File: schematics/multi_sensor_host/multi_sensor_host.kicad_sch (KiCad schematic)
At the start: 82 parts, among them J1 left hand 0, J10 swd, J11 stm_boot, J13 right hand 0, J14 right hand 1, J15 right hand 2, J16 right hand 3, J17 rst_mcu, J18 left hand 3, J19 left leg 0, J2 left hand 1, J20 left leg 1, J21 right lef 0, J22 right leg 1, J3 bm_cfg, J4 left hand 2, J5 tx, J6 MY_USB_B, J7 rst_bm71, J8 rx, J9 uart1, U11 MCP111, U12 BM71BLES1FC2-0B02AA, U4 MCP111, U7 MCP1603, U8 MCP73812, U9 MCP1603, Y1 Crystal

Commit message: Making changes...
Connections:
- net lh_int_0_0 is gone; now on net sda_1: J1.4
- net lh_int_0_1 is gone; now on net scl_1: J1.7
- net lh_int_1_0 is gone; now on net sda_3: J2.4
- net lh_int_1_1 is gone; now on net scl_3: J2.7
- net lh_int_2_0 is gone; now on net sda_5: J4.4
- net lh_int_2_1 is gone; now on net scl_5: J4.7
- net lh_int_3_0 is gone; now on net sda_7: J18.4
- net lh_int_3_1 is gone; now on net scl_7: J18.7
- net lh_scl_0 is gone; now on net scl_0: J1.3
- net lh_scl_1 is gone; now on net scl_2: J2.3
- net lh_scl_2 is gone; now on net scl_4: J4.3
- net lh_scl_3 is gone; now on net scl_6: J18.3
- net lh_sda_0 is gone; now on net sda_0: J1.1
- net lh_sda_1 is gone; now on net sda_2: J2.1
- net lh_sda_2 is gone; now on net sda_4: J4.1
- net lh_sda_3 is gone; now on net sda_6: J18.1
- net ll_int_0_0 is gone; now on net sda_17: J19.4
- net ll_int_0_1 is gone; now on net scl_17: J19.7
- net ll_int_1_0 is gone; now on net sda_19: J20.4
- net ll_int_1_1 is gone; now on net scl_19: J20.7
- net ll_scl_0 is gone; now on net scl_16: J19.3
- net ll_scl_1 is gone; now on net scl_18: J20.3
- net ll_sda_0 is gone; now on net sda_16: J19.1
- net ll_sda_1 is gone; now on net sda_18: J20.1
- net rh_int_0_0 is gone; now on net sda_9: J13.4
- net rh_int_0_1 is gone; now on net scl_9: J13.7
- net rh_int_1_0 is gone; now on net sda_11: J14.4
- net rh_int_1_1 is gone; now on net scl_11: J14.7
- net rh_int_2_0 is gone; now on net sda_13: J15.4
- net rh_int_2_1 is gone; now on net scl_13: J15.7
- net rh_int_3_0 is gone; now on net sda_15: J16.4
- net rh_int_3_1 is gone; now on net scl_15: J16.7
- net rh_scl_0 is gone; now on net scl_8: J13.3
- net rh_scl_1 is gone; now on net scl_10: J14.3
- net rh_scl_2 is gone; now on net scl_12: J15.3
- net rh_scl_3 is gone; now on net scl_14: J16.3
- net rh_sda_1 is gone; now on net sda_10: J14.1
- net rh_sda_2 is gone; now on net sda_12: J15.1
- net rh_sda_3 is gone; now on net sda_14: J16.1
- net rl_int_0_0 is gone; now on net sda_21: J21.4
- net rl_int_0_1 is gone; now on net scl_21: J21.7
- net rl_int_1_0 is gone; now on net sda_23: J22.4
- net rl_int_1_1 is gone; now on net scl_23: J22.7
- net rl_scl_0 is gone; now on net scl_20: J21.3
- net rl_scl_1 is gone; now on net scl_22: J22.3
- net rl_sda_0 is gone; now on net sda_20: J21.1
- net rl_sda_1 is gone; now on net sda_22: J22.1
- net rh_sda_0 renamed sca_8
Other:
- moved on the sheet: J1, J18, J19, J2, J20, J4, J5, J8

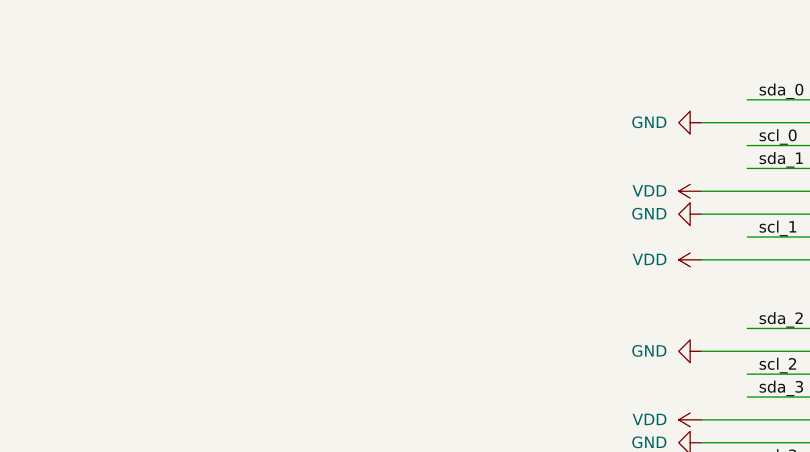
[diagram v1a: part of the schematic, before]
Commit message: 3 I2C bus, adding capacitors to sensor power lines...
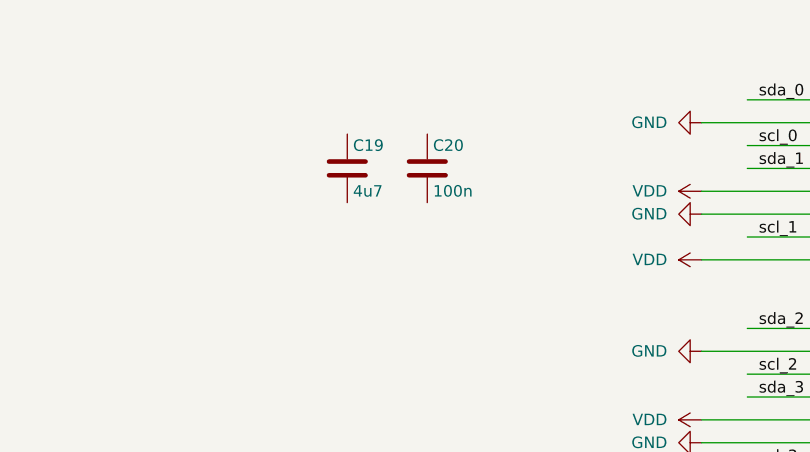
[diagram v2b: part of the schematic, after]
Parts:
- added C19: 4u7, Capacitor_SMD:C_0603_1608Metric, symbol Device:C
- added C20: 100n, Capacitor_SMD:C_0603_1608Metric, symbol Device:C
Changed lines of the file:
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@@
 	(symbol
 		(lib_id "Device:C")
+		(at 584.2 33.02 0)
+		(unit 1)
+		(exclude_from_sim no)
+		(in_bom yes)
+		(on_board yes)
+		(dnp no)
+		(property "Reference" "C19"
+			(at 584.835 30.48 0)
+			(effects
+				(font
+					(size 1.27 1.27)
+				)
+				(justify left)
+			)
+		)
+		(property "Value" "4u7"
+			(at 584.835 35.56 0)
+			(effects
+				(font
+					(size 1.27 1.27)
+				)
+				(justify left)
+			)
+		)
+		(property "Footprint" "Capacitor_SMD:C_0603_1608Metric"
+			(at 585.1652 36.83 0)
+			(effects
+				(font
+					(size 1.27 1.27)
+				)
+				(hide yes)
+			)
+		)
+		(property "Datasheet" "~"
+			(at 584.2 33.02 0)
+			(effects
+				(font
+					(size 1.27 1.27)
+				)
+				(hide yes)
+			)
+		)
+		(property "Description" "Unpolarized capacitor"
+			(at 584.2 33.02 0)
+			(effects
+				(font
+					(size 1.27 1.27)
+				)
+				(hide yes)
+			)
+		)
+		(property "URL" "https://www.digikey.com/product-detail/en/samsung-electro-mechanics-america-inc/CL10B475KQ8NQNC/1276-2087-1-ND/3890173"
+			(at 584.2 33.02 0)
+			(effects
+				(font
+					(size 1.524 1.524)
+				)
+				(hide yes)
+			)
+		)
+		(pin "1"
+		)
+		(pin "2"
+		)
+		(instances
+			(project "multi_sensor_host"
+				(path "/895fe915-d6d4-4da2-a6ec-6414a345dc15"
+					(reference "C19")
+					(unit 1)
+				)
+			)
+		)
+	)
+	(symbol
+		(lib_id "Device:C")
 		(at 424.18 140.97 0)
 		(unit 1)
@@
 					(unit 1)
 				)
+			)
+		)
+	)
+	(symbol
+		(lib_id "Device:C")
+		(at 593.09 33.02 0)
+		(unit 1)
+		(exclude_from_sim no)
+		(in_bom yes)
+		(on_board yes)
+		(dnp no)
+		(property "Reference" "C20"
+			(at 593.725 30.48 0)
+			(effects
+				(font
+					(size 1.27 1.27)
+				)
+				(justify left)
+			)
+		)
+		(property "Value" "100n"
+			(at 593.725 35.56 0)
+			(effects
+				(font
+					(size 1.27 1.27)
+				)
+				(justify left)
+			)
+		)
+		(property "Footprint" "Capacitor_SMD:C_0603_1608Metric"
+			(at 594.0552 36.83 0)
+			(effects
+				(font
+					(size 1.27 1.27)
+				)
+				(hide yes)
+			)
+		)
+		(property "Datasheet" "~"
+			(at 593.09 33.02 0)
+			(effects
+				(font
+					(size 1.27 1.27)
+				)
+				(hide yes)
+			)
+		)
+		(property "Description" "Unpolarized capacitor"
+			(at 593.09 33.02 0)
+			(effects
+				(font
+					(size 1.27 1.27)
+				)
+				(hide yes)
+			)
+		)
+		(pin "2"
+		)
+		(pin "1"
+		)
+		(instances
+			(project "multi_sensor_host"
+				(path "/895fe915-d6d4-4da2-a6ec-6414a345dc15"
+					(reference "C20")
+					(unit 1)
+				)

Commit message: All I2C multiplexers have the same address selection pins configuration. Added 22u capacitors.
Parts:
- removed C35: 4u7, Capacitor_SMD:C_0603_1608Metric, symbol Device:C
- added C25, C36, C38, C40, C42, C44, C46, C48, C50, C52, C54, C56, C58, C60, C62, C64, C66, C68, C70, C72, C74, C76, C78: 4u7, Capacitor_SMD:C_0603_1608Metric, symbol Device:C
- added C26, C37, C39, C41, C43, C45, C47, C49, C51, C53, C55, C57, C59, C61, C63, C65, C67, C69, C71, C73, C75, C77, C79: 100n, Capacitor_SMD:C_0603_1608Metric, symbol Device:C
- added C80: 22u, Capacitor_SMD:C_0603_1608Metric, symbol Device:C
- C10, C33, C34, C6: value 4u7 -> 22u; URL https://www.digikey.com/product-detail/en/samsung-electro-m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 -> https://www.digikey.com/en/products/detail/kyocera-avx/0603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
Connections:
- net GND: now also C19.2, C20.2, C25.2, C26.2, C36.2, C37.2, C38.2, C39.2, C40.2, C41.2, C42.2, C43.2, C44.2, C45.2, C46.2, C47.2, C48.2, C49.2, C50.2, C51.2, C52.2, C53.2, C54.2, C55.2, C56.2, C57.2, C58.2, C59.2, C60.2, C61.2, C62.2, C63.2, C64.2, C65.2, C66.2, C67.2, C68.2, C69.2, C70.2, C71.2, C72.2, C73.2, C74.2, C75.2, C76.2, C77.2, C78.2, C79.2, C80.2
- net VCC: now also R96.1, C80.1
- net VDD: now also C19.1, C20.1, C25.1, C26.1, C36.1, C37.1, C38.1, C39.1, C40.1, C41.1, C42.1, C43.1, C44.1, C45.1, C46.1, C47.1, C48.1, C49.1, C50.1, C51.1, C52.1, C53.1, C54.1, C55.1, C56.1, C57.1, C58.1, C59.1, C60.1, C61.1, C62.1, C63.1, C64.1, C65.1, C66.1, C67.1, C68.1, C69.1, C70.1, C71.1, C72.1, C73.1, C74.1, C75.1, C76.1, C77.1, C78.1, C79.1; no longer R96.1
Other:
- note removed: "Left arm"
- note removed: "Left leg"
- note removed: "Right arm"
- note removed: "Right leg"
- moved on the sheet: C15, C16, C17, C18, C19, C20, C21, C22, C23, C24, C27, C28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

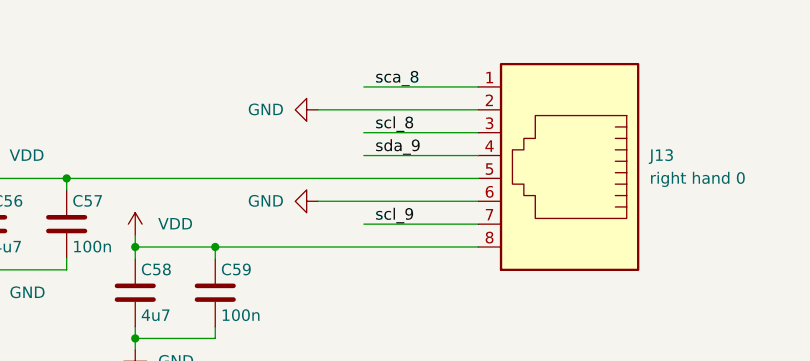
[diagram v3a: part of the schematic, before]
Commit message: Removing old wires.
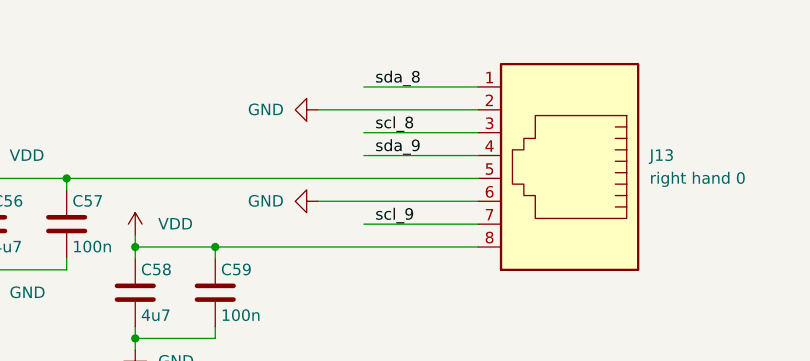
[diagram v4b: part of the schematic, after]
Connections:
- net sca_8 is gone; now on net sda_8: J13.1
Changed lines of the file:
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@@
 		)
 	)
-	(label "sca_8"
+	(label "sda_8"
 		(at 753.11 21.59 0)
 		(fields_autoplaced yes)

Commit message: Upgraded to KiCad9.0.
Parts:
- U10: symbol stm32f405rgt6_2:STM32F405RGT6 -> stm32f405rgt6:STM32F405RGT6
- U12: symbol BM71BLES1FC2:BM71BLES1FC2-0B02AA -> BM71:BM71BLES1FC2-0B02AA
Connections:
- no-connect marks 36 -> 60

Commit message: Replaced buck with low drop linear for the bluetooth.
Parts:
- removed C25, C38, C42, C46, C50, C54, C58, C62, C66, C70, C74, C78: 4u7, Capacitor_SMD:C_0603_1608Metric, symbol Device:C
- removed C26, C39, C43, C47, C51, C55, C59, C63, C67, C71, C75, C79: 100n, Capacitor_SMD:C_0603_1608Metric, symbol Device:C
- removed L2: 4.7uH, Inductor_SMD:L_1008_2520Metric, symbol Device:L
- removed U7: MCP1603, Package_TO_SOT_SMD:SOT-23-5_HandSoldering, symbol mcp1603:MCP1603T-330I/OS
- added C35: 10n, Capacitor_SMD:C_0603_1608Metric, symbol Device:C
- added U5: TPS79333-EP, Package_TO_SOT_SMD:SOT-23-5, symbol Regulator_Linear:TPS79333-EP
- C17, C18: URL (none) -> https://www.digikey.com/product-detail/en/yageo/CC0603KRX7R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
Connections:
- net GND: now also C35.2, U5.2 (GND)
- net VCC: now also U5.5 (OUT)
- net Vin: now also U5.1 (IN), U5.3 (EN)
- new net: C35.1, U5.4 (BP)
- no-connect marks 60 -> 59
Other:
- moved on the sheet: C5, C80

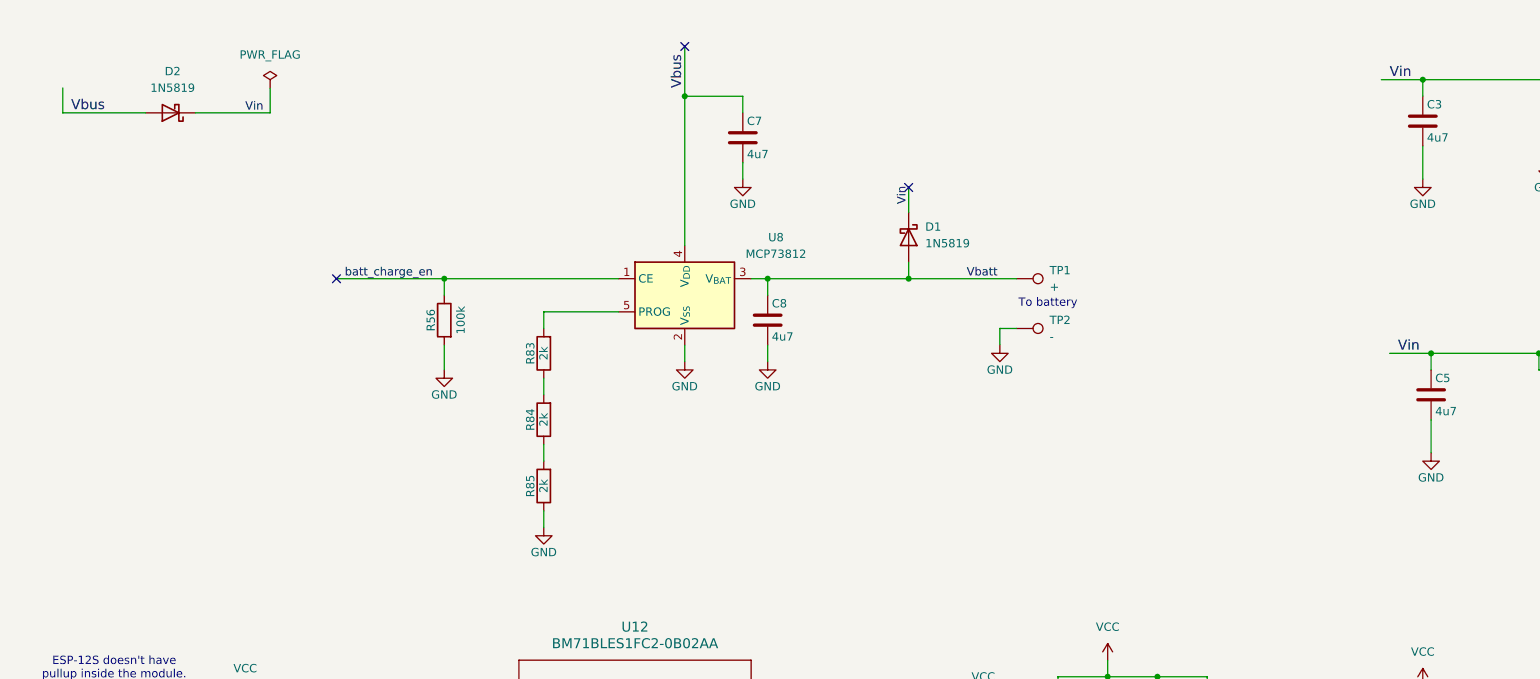
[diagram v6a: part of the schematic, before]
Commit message: Groupping different logical component groups to move them together.
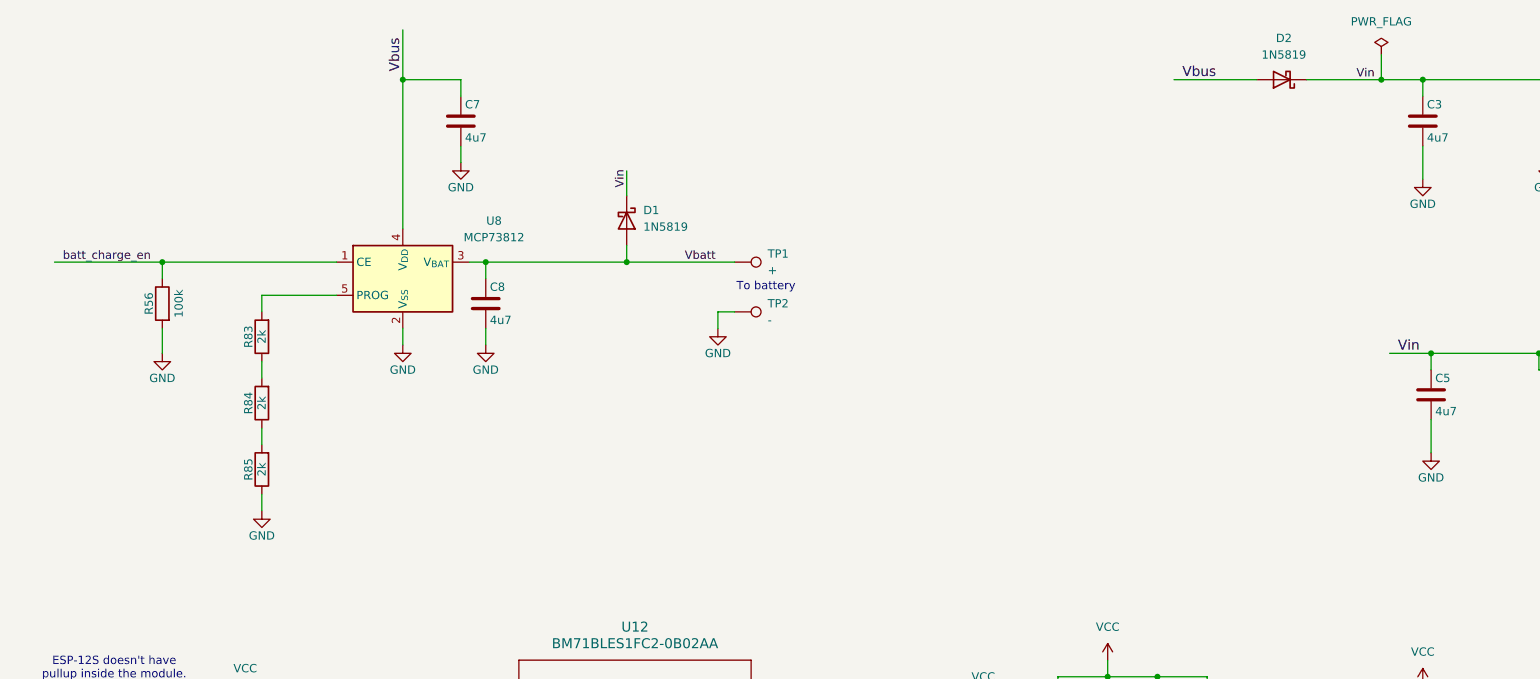
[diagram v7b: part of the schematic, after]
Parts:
- TP1, TP2: footprint TestPoint:TestPoint_Pad_D4.0mm -> Connector_PinHeader_1.00mm:PinHeader_1x01_P1.00mm_Vertical
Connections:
- no-connect marks 59 -> 56
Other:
- moved on the sheet: C7, C8, D1, D2, R56, R83, R84, R85, TP1, TP2, U8

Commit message: a
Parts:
- TP1, TP2: footprint Connector_PinHeader_1.00mm:PinHeader_1x01_P1.00mm_Vertical -> Connector_Pin:Pin_D1.4mm_L8.5mm_W2.8mm_FlatFork
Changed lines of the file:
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@@
 			)
 		)
-		(property "Footprint" "Connector_PinHeader_1.00mm:PinHeader_1x01_P1.00mm_Vertical"
+		(property "Footprint" "Connector_Pin:Pin_D1.4mm_L8.5mm_W2.8mm_FlatFork"
 			(at 121.92 63.5 0)
 			(effects
@@
 			)
 		)
-		(property "Footprint" "Connector_PinHeader_1.00mm:PinHeader_1x01_P1.00mm_Vertical"
+		(property "Footprint" "Connector_Pin:Pin_D1.4mm_L8.5mm_W2.8mm_FlatFork"
 			(at 121.92 55.88 0)
 			(effects
